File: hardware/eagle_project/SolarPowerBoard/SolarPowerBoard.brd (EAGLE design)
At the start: 68.8 x 53.6 mm, 83 parts, among them IC1 BQ29700DSET_BQ29700DSET, IC3 TPS63031DSKT_TPS63031DSKT, J2 105017-0001_105017-0001, J5 XG8S-0331_XG8S-0331, K1 G6E-134P-US_DC5_G6E-134P-US_D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, Q3 DAVIDE_FDN302P, U4 MCP73831T-2ACI_OT_MCP73831T-2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

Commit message: commiting the PCB printed ad eurocircuit (very first version)
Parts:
- removed C1-1, C1-2: 4.7uF, SolarPowerBoard:SPARKFUN-CAPACITORS_0603
- removed CHG2: SOLARCOMPONENTS_CSD16406Q3, SolarPowerBoard:SOLARCOMPONENTS_CSD16327
- removed D5: RED, SolarPowerBoard:SPARKFUN-LED_LED-0603
- removed IC1: BQ29700DSET_BQ29700DSET, SolarPowerBoard:BQ29700DSET_SON50P150X150X80-6N
- removed RCG3: KRL2012E-C-R020-F, SolarPowerBoard:RESC1216X70N
- removed RX: ORANGE, SparkFun-LED:LED-0603
- removed TX: YELLOW, SparkFun-LED:LED-0603
- added C13: 10u, SolarPowerBoard:SPARKFUN-CAPACITORS_0805
- added LED_CH, LED_RX, LED_TX: (no value), SolarPowerBoard:LED-0603
- added Q1: (no value), SolarPowerBoard:SOLARCOMPONENTS_CSD16327
- added R5: 0.02, SolarPowerBoard:FCSL90R020DER_FOOTPRINT
- added U6: MCP73831T-2ACI_OT_MCP73831T-2ACI/OT, SolarPowerBoard:MCP73831T-2ACI_OT_SOT95P280X145-5N
- C1, C5, C7, CMPP: value 0.1uF -> 100n; device SolarPowerBoard:SPARKFUN-CAPACITORS_0603 -> SolarPowerBoard:SPARKFUN-CAPACITORS_0805
- C10: value 470nF -> 470n; device SolarPowerBoard:RESISTOR_C0805 -> SolarPowerBoard:SPARKFUN-CAPACITORS_0805
- C11, C12: device SolarPowerBoard:SPARKFUN-CAPACITORS_0603-CAP -> SolarPowerBoard:SPARKFUN-CAPACITORS_0805
- C14: value 10nF -> 10n
- C15, C16: value 47pF -> 47p
- C2, C3, C4: value 10uF -> 10u
- C24, C26, C8, C9: value 100nF -> 100n
- C25: value 4.7uF -> 4.7u
- C6: value 470pF -> 470p; device SolarPowerBoard:SPARKFUN-CAPACITORS_0603 -> SolarPowerBoard:SPARKFUN-CAPACITORS_0805
- CF: value 1.0uF -> 1.0u
- COUT1: value 10uF -> 10u; device SolarPowerBoard:RESISTOR_C0805 -> SolarPowerBoard:SPARKFUN-CAPACITORS_0805
- COUT2: value 33uF -> 33u; device SolarPowerBoard:RESISTOR_C0805 -> SolarPowerBoard:SPARKFUN-CAPACITORS_0805
- J2: value 105017-0001_105017-0001 -> (none)
- J3: value (none) -> BAT_ID
- J5: value XG8S-0331_XG8S-0331 -> (none)
- JP1: value SPARKFUN-JUMPERS_JUMPER-SMT_3_1-NC_TRACE_NO-SILK -> (none)
- K1: value G6E-134P-US_DC5_G6E-134P-US_DC5 -> (none)
- L1: value EMC9714 -> 27u; device inductors:EMC9714 -> SolarPowerBoard:AXIAL-14MM
- L2: value SRN3010-470M_SRN3010-470M -> 47u
- L3: value MI0805K601R-10 -> (none)
- Q2: value SOLARCOMPONENTS_CSD16406Q3 -> (none)
- R1, R2, R3, R8, RF1, RF2: device SolarPowerBoard:RESISTOR_R0805 -> SolarPowerBoard:SPARKFUN-RESISTORS_0805:1
- R27, R28: value 470 -> 680; device SparkFun-Resistors:0805 -> SolarPowerBoard:SPARKFUN-RESISTORS_0805:1
- RGPIO1, RGPIO2, RGPIO3, RGPIO4: value (none) -> 1k; device SolarPowerBoard:SPARKFUN-RESISTORS_0603:2 -> SolarPowerBoard:SPARKFUN-RESISTORS_0805:1
- RGS1, RGS2: value 5MOhm -> 5M; device SolarPowerBoard:RESISTOR_R0805 -> SolarPowerBoard:SPARKFUN-RESISTORS_0805:2
- RLED1, RPROG1: device SolarPowerBoard:SPARKFUN-PASSIVES_0603-RES -> SolarPowerBoard:SPARKFUN-RESISTORS_0805:1
- RRX: value 0 -> 1k; device resistor:R0805 -> SolarPowerBoard:SPARKFUN-RESISTORS_0805:1
- RS1: value RL1220T-R010-J_RL1220T-R010-J -> 0.01
- RTEMP: device SolarPowerBoard:RESISTOR_R0805 -> SolarPowerBoard:SPARKFUN-RESISTORS_0805:2
- U1: value SOLARCOMPONENTS_SVP1040 -> (none)
- U2: value SOLARCOMPONENTS_MAX17260 -> (none)
- U3: value FT230XQ-R -> (none)
- U4: value MCP73831T-2ACI_OT_MCP73831T-2ACI/OT -> (none); device SolarPowerBoard:MCP73831T-2ACI_OT_SOT95P280X145-5N -> SolarPowerBoard:BQ29700DSET_SON50P150X150X80-6N
- U5: value TPS63031DSKT_TPS63031DSKT -> (none)
- U7: value 74XX-LITTLE-DE_74AHC1G08DCK -> (none)
- moved U4 25.5 mm to (15.6, 26.0), turned to 270 degrees
- moved R10 10.9 mm to (14.3, 22.7), turned to 0 degrees
- moved R9 10.6 mm to (16.9, 22.8), turned to 270 degrees
- moved R4 9.54 mm to (21.9, 42.1), turned to 180 degrees
- moved C11 8.04 mm to (34.1, 32.1), turned to 180 degrees
- moved C12 8.03 mm to (42.2, 34.1), turned to 270 degrees
- moved COUT2 6.23 mm to (28.7, 22.6)
- moved C7 6.14 mm to (17.3, 35.4), turned to 0 degrees
- moved RGPIO1 3.14 mm to (50.4, 5.69), turned to 90 degrees
- moved RGS1 3.05 mm to (10.7, 13.5), turned to 90 degrees
- moved J5 2.79 mm to (54.8, 15.9), turned to 270 degrees
- moved COUT1 2.29 mm to (29.6, 17.2), turned to 0 degrees
- moved RGPIO4 2.28 mm to (58.0, 5.64), turned to 90 degrees
- moved RS1 2.06 mm to (28.7, 19.5)
- moved R1 1.80 mm to (21.2, 18.4)
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- renumbered AND to U7, DCH2 to Q2, FT230XQ-R to U3, IC3 to U5, RB2 to B1, U$1 to U1, U$2 to B2, U$3 to U2
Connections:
- net DP4_UART_FTDI_TX renamed FTDI_TX
- removed net N$23: K1.6
- new net FTDI_RX: RRX.2, RX_TX.2, U3.2
- net BAT_DETECTION: now also RTEMP.1; no longer RTEMP.2
- net DP5_UART_FTDI_RX: no longer RRX.2, RX_TX.2, U3.2
- net GND: now also C10.1, C13.2, COUT1.2, COUT2.2, K1.6, Q1.1, Q1.2, Q1.3, U6.2; no longer C1-1.2, C1-2.2, C10.2, CHG2.1, CHG2.2, CHG2.3, COUT1.1, COUT2.1, U4.2
- net GPIO1: now also RGPIO1.1; no longer RGPIO1.2
- net GPIO2: now also RGPIO2.1; no longer RGPIO2.2
- net GPIO3: now also RGPIO3.1; no longer RGPIO3.2
- net GPIO4: now also RGPIO4.1; no longer RGPIO4.2
- net N$1: now also C13.1, L1.P$1, R3.2; no longer C1-1.1, C1-2.1, L1.1, R3.1
- net N$13: now also RLED1.2, U6.1; no longer RLED1.1, U4.1
- net N$14: now also Q1.5, Q1.6, Q1.7, Q1.8, Q1.9; no longer CHG2.5, CHG2.6, CHG2.7, CHG2.8, CHG2.9
- net N$15: now also Q1.4, U4.2; no longer CHG2.4, IC1.2
- net N$18: now also L1.P$2; no longer L1.2
- net N$19: now also U4.4; no longer IC1.4
- net N$2: now also U6.5; no longer U4.5
- net N$20: now also C11.1, U6.3; no longer C12.1, U4.3
- net N$21: now also RTEMP.2; no longer RTEMP.1
- net N$22: now also U4.3; no longer IC1.3
- net N$24: now also U4.5; no longer IC1.5
- net N$28: now also RGPIO1.2; no longer RGPIO1.1
- net N$29: now also U4.6; no longer IC1.6
- net N$3: now also R3.1, R8.2; no longer R3.2, R8.1
- net N$30: now also RGPIO2.2; no longer RGPIO2.1
- net N$31: now also R28.2; no longer R28.1
- net N$32: now also LED_RX.C, R28.1; no longer R28.2, RX.C
- net N$33: now also RGPIO3.2; no longer RGPIO3.1
- net N$4: now also R8.1; no longer R8.2
- net N$41: now also RGPIO4.2; no longer RGPIO4.1
- net N$42: now also LED_TX.C, R27.1; no longer R27.2, TX.C
- net N$43: now also R27.2; no longer R27.1
- net N$45: now also C10.2; no longer C10.1
- net N$5: now also COUT1.1, RF1.1; no longer COUT1.2, RF1.2
- net N$6: now also RF1.2; no longer RF1.1
- net N$7: now also RF2.2; no longer RF2.1
- net N$9: now also LED_CH.C, RLED1.1; no longer D5.C, RLED1.2
- net PACK+: now also R5.2; no longer RCG3.2
- net POWER_INPUT: now also R5.1; no longer RCG3.1
- net SOLAR_OUTPUT: now also COUT2.1, RF2.1; no longer COUT2.2, RF2.2
- net VCCIO_FTDI: now also LED_RX.A, LED_TX.A; no longer RX.A, TX.A
- net VDD_CHARGER: now also C12.1, LED_CH.A, U6.4; no longer C11.1, D5.A, U4.4
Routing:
- net FTDI_RX: track 0.00 -> 28.4 mm, vias 0 -> 2
- net DP5_UART_FTDI_RX: track 30.5 -> 2.18 mm, vias 2 -> 0
- net GND: track 44.5 -> 22.4 mm, vias 156 -> 155
- net N$29: track 20.6 -> 2.42 mm
- net N$9: track 18.3 -> 2.55 mm
- net VDD_CHARGER: track 54.2 -> 39.2 mm
- net N$24: track 17.1 -> 4.81 mm, vias 2 -> 0
- net N$14: track 9.38 -> 0.00 mm, vias 0 -> 6
- net SOLAR_OUTPUT: track 61.9 -> 52.5 mm, vias 1 -> 0
- net PACK+: track 43.5 -> 52.1 mm, vias 4 -> 0
- net N$5: track 13.2 -> 5.44 mm
- net N$11: track 2.50 -> 9.79 mm
- net N$1: track 34.8 -> 28.4 mm
- net SCL_FG: track 75.8 -> 69.8 mm
- net N$10: track 11.8 -> 6.70 mm
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- added copper zone on layer 1, net N$14
- added copper zone on layer 16, net N$14
- added copper zone on layer 1, net N$5
- added copper zone on layer 1, net SOLAR_OUTPUT
- added copper zone on layer 1, net VDD
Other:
- board text added: "BAT_ID_CFG"
- board text added: "BYPASS"
- board text added: "CC"
- board text added: "CTS"
- board text added: "EN"
- board text added: "FG"
- board text added: "FG_I2C"
- board text added: "FTDI"
- board text added: "MPPT_BYPASS"
- board text added: "PANEL"
- board text added: "RTS"
- board text added: "USB_CHARGING"
- board text added: "nRF"
- board text removed: "DIRECT"
- board text removed: "Harvester"
- board text removed: "IN"
- board text removed: "SOLAR"
- board text removed: "USB-CHARGING"

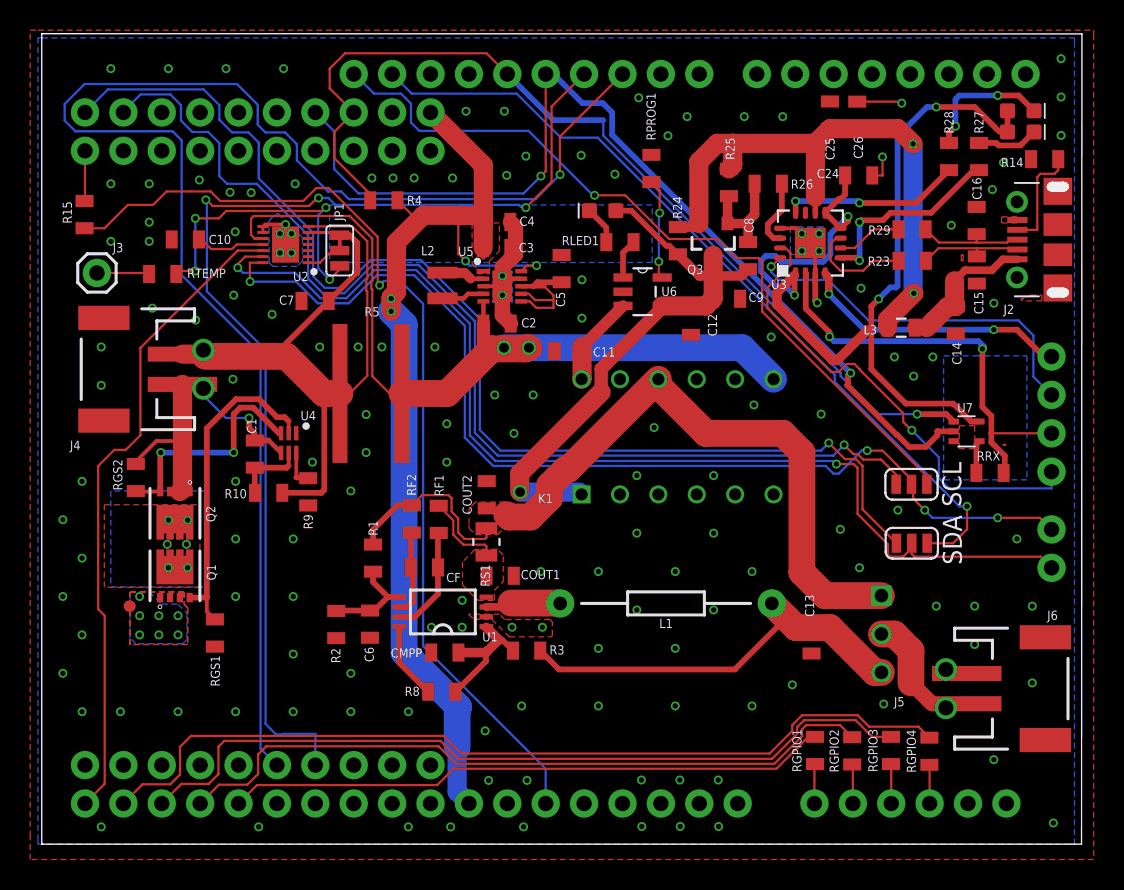
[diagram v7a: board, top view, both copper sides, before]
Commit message: PCB project update
- arduino header fix
- text fix
- library refactor (now all the capacitor use the same component as well as resistors)
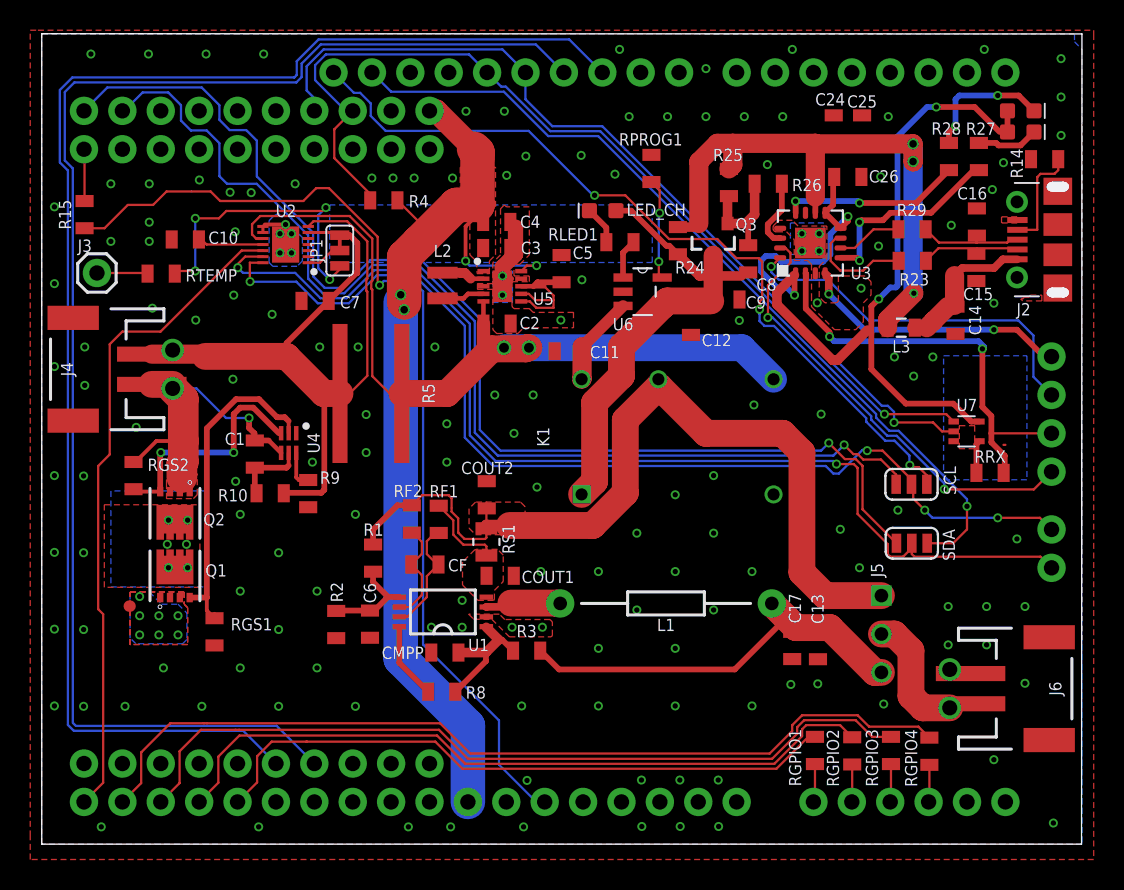
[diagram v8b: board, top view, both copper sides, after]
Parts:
- added C17: 4.7u, SolarPowerBoard:SPARKFUN-CAPACITORS_0805
- C13: value 10u -> 4.7u
- C14, C15, C16, C24, C25, C26, C8, C9: device SolarPowerBoard:SPARKFUN-CAPACITORS_0805:1 -> SolarPowerBoard:SPARKFUN-CAPACITORS_0805
- CF: value 1.0u -> 1u
- J2: value (none) -> 105017-0001_105017-0001
- J5: value (none) -> XG8S-0331_XG8S-0331
- JP1: value (none) -> SPARKFUN-JUMPERS_JUMPER-SMT_3_1-NC_TRACE_NO-SILK
- K1: value (none) -> G6E-134P-US_DC5_G6E-134P-US_DC5
- L3: value (none) -> DAVIDE_FERRITE_BREAD
- Q1, Q2: value (none) -> SOLARCOMPONENTS_CSD16406Q3
- R1, R14, R15, R2, R23, R24, R25, R26, R27, R28, R29, R3, R4, R8, RF1, RF2, RGPIO1, RGPIO2, RGPIO3, RGPIO4, RPROG1, RRX: device SolarPowerBoard:SPARKFUN-RESISTORS_0805:1 -> SolarPowerBoard:SPARKFUN-RESISTORS_0805
- R10, R9, RGS1, RGS2, RTEMP: device SolarPowerBoard:SPARKFUN-RESISTORS_0805:2 -> SolarPowerBoard:SPARKFUN-RESISTORS_0805
- RLED1: value 680 -> 1k; device SolarPowerBoard:SPARKFUN-RESISTORS_0805:1 -> SolarPowerBoard:SPARKFUN-RESISTORS_0805
- U1: value (none) -> SOLARCOMPONENTS_SVP1040
- U2: value (none) -> SOLARCOMPONENTS_MAX17260
- U3: value (none) -> FT230XQ_FT230XQ_2
- U4: value (none) -> BQ29700DSET_BQ29700DSET
- U5: value (none) -> TPS63031DSKT_TPS63031DSKT
- U7: value (none) -> 74XX-LITTLE-DE_74AHC1G08DCK
- moved B2 35.8 mm to (63.0, 2.29)
- moved B1 34.7 mm to (24.9, 48.0)
- moved C26 4.13 mm to (52.6, 43.6), turned to 0 degrees
- moved C24 3.49 mm to (51.6, 46.8), turned to 90 degrees
- moved C25 2.31 mm to (53.5, 46.8)
- moved J4 2.03 mm to (2.82, 30.9)
- moved C13 0.57 mm to (50.6, 12.6)
- moved J6 0.25 mm to (64.4, 9.78)
- moved C8 0.21 mm to (46.0, 38.2)
- moved CF 0.20 mm to (24.6, 18.0)
- moved RGS2 0.20 mm to (5.31, 23.9), turned to 270 degrees
- moved C15 0.17 mm to (61.1, 37.6)
- moved R9 0.12 mm to (16.9, 22.7)
- moved RTEMP 0.10 mm to (7.14, 37.2), turned to 180 degrees
- moved R10 0.10 mm to (14.4, 22.7), turned to 180 degrees
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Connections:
- net BAT_DETECTION: now also RTEMP.2; no longer RTEMP.1
- net GND: now also C17.2, RGS1.2; no longer RGS1.1
- net N$1: now also C17.1
- net N$15: now also RGS1.1; no longer RGS1.2
- net N$19: now also RGS2.1; no longer RGS2.2
- net N$21: now also RTEMP.1; no longer RTEMP.2
- net N$22: now also RGS2.2; no longer RGS2.1
- net N$24: now also R10.2; no longer R10.1
- net PACK+: now also R10.1; no longer R10.2
- net VCCIO_FTDI: now also C26.1; no longer C24.1
- net VCC_FTDI: now also C24.1; no longer C26.1
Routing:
- net PO.23(RTS)-DIO19(CTS): track 74.2 -> 94.7 mm, vias 3 -> 0
- net GND: track 22.4 -> 7.20 mm, vias 155 -> 165
- net VDD_CHARGER: track 39.2 -> 32.0 mm, vias 1 -> 0
- net PO.24(TX)-DIO2(RX): track 65.4 -> 58.3 mm, vias 2 -> 1
- net SOLAR_OUTPUT: track 52.5 -> 57.3 mm
- net PO.22(CTS)-DIO18(RTS): track 100.2 -> 95.8 mm, vias 1 -> 0
- net VDD: track 69.3 -> 65.3 mm
- net N$28: track 40.0 -> 42.5 mm
- net N$39: track 52.1 -> 54.4 mm, vias 1 -> 3
- net PACK+: track 52.1 -> 54.3 mm
- net PO.25(RX)-DIO3(TX): track 63.4 -> 65.1 mm
- net N$38: track 54.7 -> 56.2 mm
- net FTDI_TX: track 31.6 -> 30.1 mm, vias 1 -> 2
- net N$7: track 5.76 -> 7.18 mm
- net VCC_FTDI: track 42.2 -> 40.8 mm, vias 2 -> 3
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- added copper zone on layer 1, net N$19
- removed copper zone on layer 1, net AFDV
